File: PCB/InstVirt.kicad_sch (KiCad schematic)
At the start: 45 parts, among them J1 Conn_01x20_Pin, J2 Conn_01x20_Pin, J3 Conn_01x08_Socket, J4 Conn_01x08_Socket, Q1 BC548, Q2 BC548, Q3 BC548, Q4 BC548, Q5 BC548, Q6 BC548, Q7 BC548, Q8 BC548, U1 4051

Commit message: Actualizo circuito PCB
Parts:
- removed Q1, Q2, Q3, Q5, Q6, Q7, Q8: BC548, Package_TO_SOT_THT:TO-92_Inline, symbol Transistor_BJT:BC548
- removed R25, R33, R34, R40, R44: R, symbol Device:R
- removed R26, R35, R37, R41, R46: 10KΩ, symbol Device:R
- added R19, R20, R23: R10KΩ, symbol Device:R
- added U2: ULN2003, symbol Transistor_Array:ULN2003
- R17, R21: value R -> R10KΩ
- R18, R22: value 10KΩ -> R10KΩ
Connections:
- net GND: now also U2.8 (GND)
- net SD1: now also R17.1, U2.16 (O1); no longer R18.1
- net SD2: now also R21.1, U2.15 (O2)
- net SD3: now also R23.1, U2.14 (O3); no longer Q4.1 (C), R30.1
- net SD4: now also R18.1, U2.13 (O4)
- net SD5: now also R20.1, U2.12 (O5); no longer R22.1
- net SD6: now also R19.1, U2.11 (O6)
- net SD8: now also Q4.1 (C), R30.1
- net VCC: now also R17.2, R21.2, R19.2, R20.2, R23.2
- net 1: now reaches R29.1
- net 1: now also U2.1 (I1), U2.2 (I2), U2.3 (I3), U2.4 (I4), U2.5 (I5), U2.6 (I6), U2.7 (I7)
- new net: R22.1, U2.10 (O7)
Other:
- moved on the sheet: J4, Q4, R29, R30

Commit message: actualizacion pcb2
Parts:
- added J5: Conn_01x08_Socket, symbol Connector:Conn_01x08_Socket
- added R24, R27, R31, R33, R35, R37, R39, R41: 10KΩ, symbol Device:R
- added R25, R26, R28, R32, R34, R36, R38, R40: R, symbol Device:R
- added U10, U3, U4, U5, U6, U7, U8, U9: PC817, Package_DIP:DIP-4_W7.62mm, symbol Isolator:PC817
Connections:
- net GND: now also R24.2, R27.2, R31.2, R33.2, R35.2, R37.2, R39.2, R41.2
- net VCC: now also U1.16 (VDD)
- new net: R40.1, U10.1
- new net: R25.1, U3.1
- new net: R36.1, U8.1
- new net: R34.1, U7.1
- new net: R38.1, U9.1
- new net: R26.1, U4.1
- new net: R28.1, U5.1
- new net: R32.1, U6.1
- new net +3.3V: U10.4, U3.4, U4.4, U5.4, U6.4, U7.4, U8.4, U9.4
- new net E1: J5.8 (Pin_8), R25.2
- new net E2: J5.7 (Pin_7), R26.2
- new net E3: J5.6 (Pin_6), R28.2
- new net E4: J5.5 (Pin_5), R32.2
- new net E5: J5.4 (Pin_4), R34.2
- new net E6: J5.3 (Pin_3), R36.2
- new net E7: J5.2 (Pin_2), R38.2
- new net E8: J5.1 (Pin_1), R40.2
- new net GND2: U10.2, U3.2, U4.2, U5.2, U6.2, U7.2, U8.2, U9.2
- new net ID1: R24.1, U3.3
- new net ID2: R27.1, U4.3
- new net ID3: R31.1, U5.3
- new net ID4: R33.1, U6.3
- new net ID5: R35.1, U7.3
- new net ID6: R37.1, U8.3
- new net ID7: R39.1, U9.3
- new net ID8: R41.1, U10.3
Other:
- note added: "ENTRADA DIGITAL 0-5 v"
- moved on the sheet: J1, J2, J4, Q4, R17, R18, R19, R20, R21, R22, R23, R29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

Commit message: actualizacion pcb3
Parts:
- added J6: Conn_01x04, Connector_PinSocket_2.54mm:PinSocket_1x04_P2.54mm_Vertical, symbol Connector_Generic:Conn_01x04
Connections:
- net A6 is gone; now on net A6ADC1_IN6: J1.10 (Pin_10)
- net B12 is gone; now on net B12EN: J2.1 (Pin_1)
- net MUXA is gone; now on net B15MUXA: U1.11 (A)
- net MUXB is gone; now on net B14MUXB: U1.10 (B)
- net MUXC is gone; now on net B13MUXC: U1.9 (C)
- net E1: no longer R25.2
- net E2: no longer R26.2
- net E3: no longer R28.2
- net E4: no longer R32.2
- net E5: no longer R34.2
- net E6: no longer R36.2
- net E7: no longer R38.2
- net E8: no longer R40.2
- net A6ADC1_IN6: now reaches U1.3 (X)
- net B12EN: now reaches U1.6 (Inh)
- removed net 1: R29.1, U2.1 (I1), U2.2 (I2), U2.3 (I3), U2.4 (I4), U2.5 (I5), U2.6 (I6), U2.7 (I7)
- net A0 renamed A0O3
- net A0O3: now also U2.5 (I5)
- net A1 renamed A1O4
- net A1O4: now also U2.4 (I4)
- net A10 renamed A10RX
- net A10RX: now also J6.2 (Pin_2)
- net A15 renamed A15ID8
- net A15ID8: now also R40.2
- net A2 renamed A2O5
- net A2O5: now also U2.3 (I3)
- net A3 renamed A3O6
- net A3O6: now also U2.2 (I2)
- net A4 renamed A4O7
- net A4O7: now also U2.1 (I1)
- net A5 renamed A5O8
- net A5O8: now also R29.1
- net A7 renamed A7OPWM1
- net A8 renamed A8RS_MODE
- net A9 renamed A9TX
- net A9TX: now also J6.3 (Pin_3)
- net B0 renamed B0OPWM2
- net B13 renamed B13MUXC
- net B14 renamed B14MUXB
- net B15 renamed B15MUXA
- net B3 renamed B3ID7
- net B4 renamed B4ID6
- net B4ID6: now also R36.2
- net B5 renamed B5ID5
- net B5ID5: now also R34.2
- net B6 renamed B6ID4
- net B6ID4: now also R32.2
- net B7 renamed B7ID3
- net B7ID3: now also R28.2
- net B8 renamed B8ID2
- net B9 renamed B9ID1
- net B9ID1: now also R25.2
- net C13: no longer names the net of J1.19 (Pin_19)
- net C14 renamed C14O1
- net C14O1: now also U2.7 (I7)
- net C15 renamed C15O2
- net C15O2: now also U2.6 (I6)
- new net B9ID2: R26.2
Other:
- moved on the sheet: Q4, R29, R30

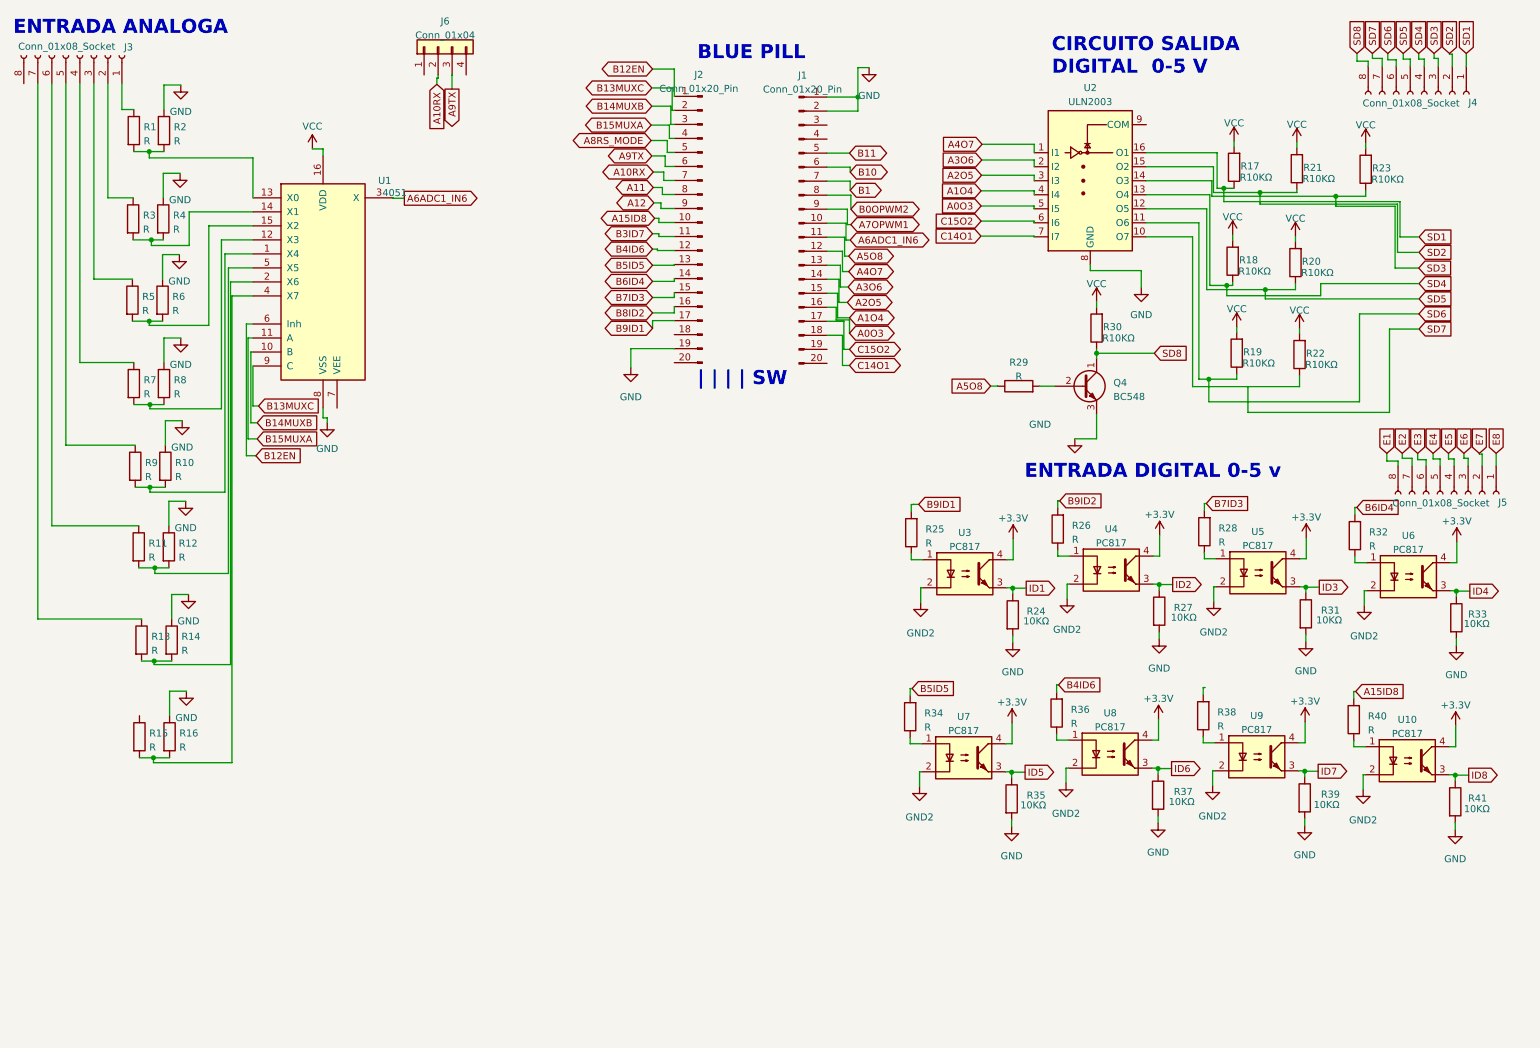
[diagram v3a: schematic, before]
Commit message: Solo faltan entradas analóogicas
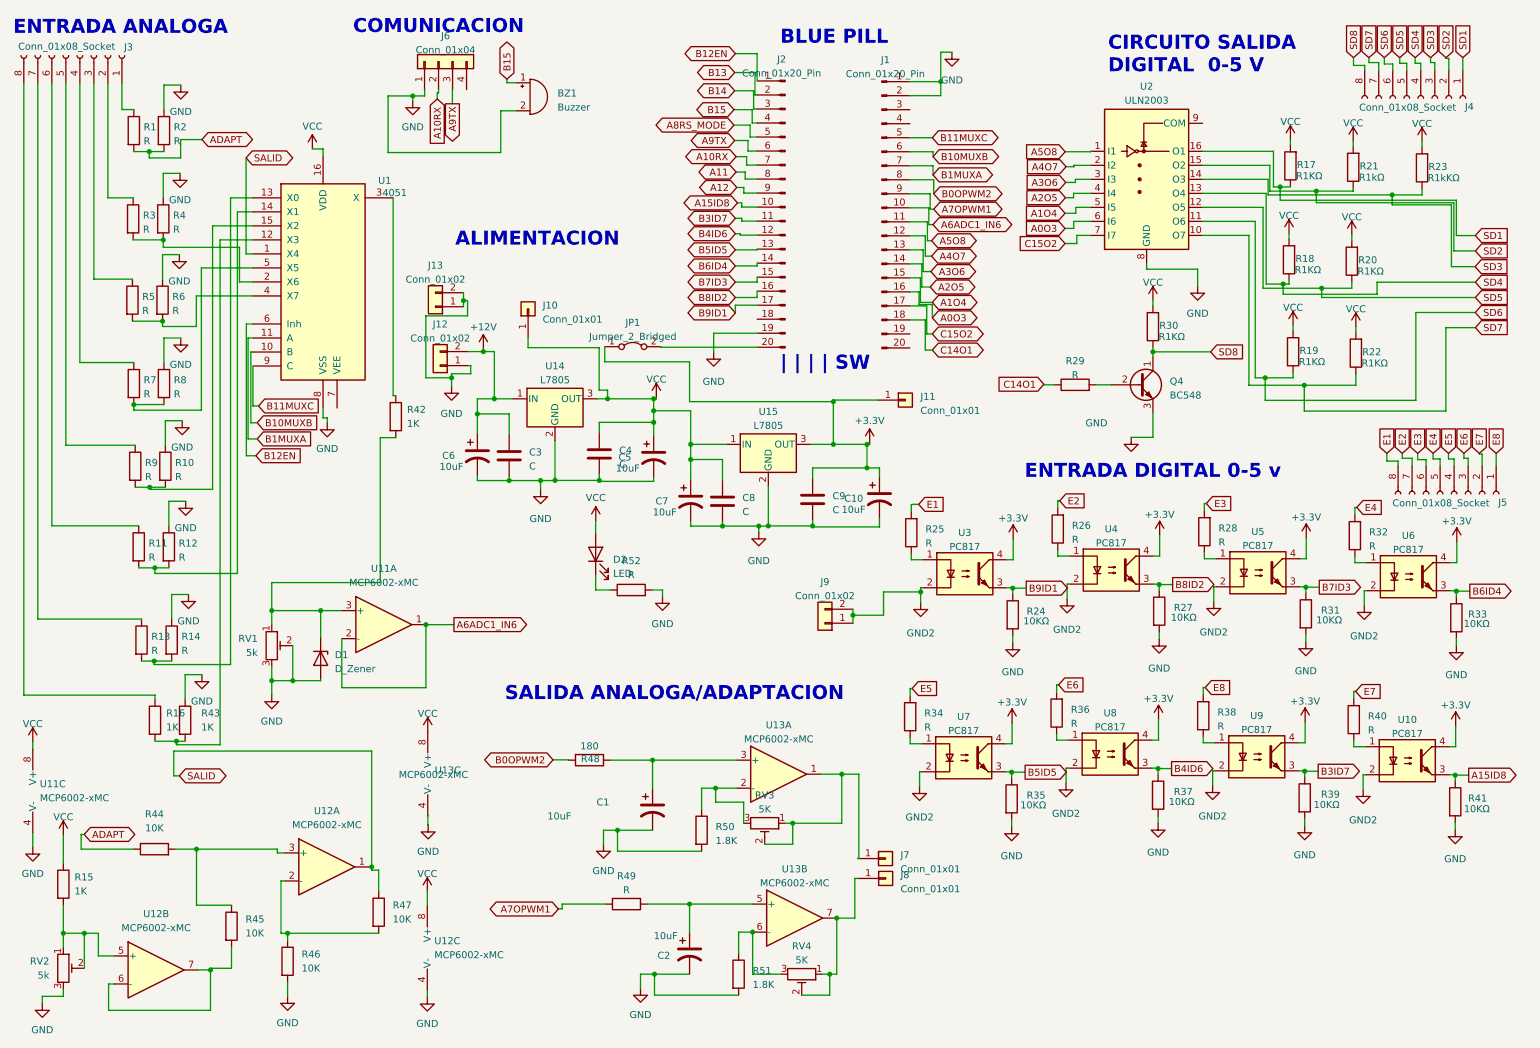
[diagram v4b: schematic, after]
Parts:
- added BZ1: Buzzer, Buzzer_Beeper:MagneticBuzzer_ProSignal_ABI-010-RC, symbol Device:Buzzer
- added C1, C10, C2, C5, C6, C7: 10uF, Capacitor_THT:CP_Radial_D5.0mm_P2.50mm, symbol Device:C_Polarized_US
- added C3, C4, C8, C9: C, Capacitor_THT:C_Disc_D5.0mm_W2.5mm_P5.00mm, symbol Device:C
- added D1: D_Zener, Diode_THT:D_DO-34_SOD68_P10.16mm_Horizontal, symbol Device:D_Zener
- added D2: LED, LED_THT:LED_D5.0mm, symbol Device:LED
- added J10, J11, J7, J8: Conn_01x01, Connector_PinSocket_2.54mm:PinSocket_1x01_P2.54mm_Vertical, symbol Connector_Generic:Conn_01x01
- added J12, J13: Conn_01x02, TerminalBlock_Phoenix:TerminalBlock_Phoenix_MKDS-1,5-2_1x02_P5.00mm_Horizontal, symbol Connector_Generic:Conn_01x02
- added J9: Conn_01x02, Connector_PinSocket_2.54mm:PinSocket_1x02_P2.54mm_Vertical, symbol Connector_Generic:Conn_01x02
- added JP1: Jumper_2_Bridged, Connector_PinSocket_2.54mm:PinSocket_1x02_P2.54mm_Vertical, symbol Jumper:Jumper_2_Bridged
- added R42: 1K, Resistor_SMD:R_1206_3216Metric, symbol Device:R
- added R43: 1K, Resistor_THT:R_Axial_DIN0207_L6.3mm_D2.5mm_P10.16mm_Horizontal, symbol Device:R
- added R44, R45, R46, R47: 10K, Resistor_SMD:R_1206_3216Metric, symbol Device:R
- added R48: 180, Resistor_SMD:R_1206_3216Metric, symbol Device:R
- added R49: R, Resistor_SMD:R_1206_3216Metric, symbol Device:R
- added R50, R51: 1.8K, Resistor_THT:R_Axial_DIN0207_L6.3mm_D2.5mm_P10.16mm_Horizontal, symbol Device:R
- added R52: R, Resistor_THT:R_Axial_DIN0207_L6.3mm_D2.5mm_P10.16mm_Horizontal, symbol Device:R
- added RV1, RV2: 5k, Potentiometer_THT:Potentiometer_Bourns_3296W_Vertical, symbol Device:R_Potentiometer_Trim
- added RV3, RV4: 5K, Potentiometer_THT:Potentiometer_Bourns_3296W_Vertical, symbol Device:R_Potentiometer_Trim
- added U11, U12, U13: MCP6002-xMC, Package_DIP:DIP-8_W7.62mm_LongPads, symbol Amplifier_Operational:MCP6002-xMC
- added U14, U15: L7805, Package_TO_SOT_THT:TO-220-3_Vertical, symbol Regulator_Linear:L7805
- J3, J5: footprint (none) -> Connector_PinHeader_2.54mm:PinHeader_1x08_P2.54mm_Vertical
- J4: footprint (none) -> Connector_PinSocket_2.54mm:PinSocket_1x08_P2.54mm_Vertical
- R1, R11, R13, R24, R27, R3, R31, R33, R35, R37, R39, R41, R5, R7, R9: footprint (none) -> Resistor_SMD:R_1206_3216Metric
- R10, R12, R14, R2, R25, R26, R28, R29, R32, R34, R36, R38, R4, R40, R6, R8: footprint (none) -> Resistor_THT:R_Axial_DIN0207_L6.3mm_D2.5mm_P10.16mm_Horizontal
- R15, R16: value R -> 1K; footprint (none) -> Resistor_SMD:R_1206_3216Metric
- R17, R18, R19, R20, R22, R30: value R10KΩ -> R1KΩ; footprint (none) -> Resistor_SMD:R_1206_3216Metric
- R21: value R10KΩ -> R1kΩ; footprint (none) -> Resistor_SMD:R_1206_3216Metric
- R23: value R10KΩ -> R1kKΩ; footprint (none) -> Resistor_SMD:R_1206_3216Metric
- U1: footprint (none) -> Package_DIP:DIP-16_W7.62mm_LongPads
- U2: footprint (none) -> Package_SO:SOP-16_4.4x10.4mm_P1.27mm
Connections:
- net B9ID2 is gone; now on net E2: R26.2
- net ID1 is gone; now on net B9ID1: R24.1, U3.3
- net ID2 is gone; now on net B8ID2: R27.1, U4.3
- net ID3 is gone; now on net B7ID3: R31.1, U5.3
- net ID4 is gone; now on net B6ID4: R33.1, U6.3
- net ID5 is gone; now on net B5ID5: R35.1, U7.3
- net ID6 is gone; now on net B4ID6: R37.1, U8.3
- net ID7 is gone; now on net B3ID7: R39.1, U9.3
- net ID8 is gone; now on net A15ID8: R41.1, U10.3
- net +3.3V: now also C10.1, C9.1, J11.1 (Pin_1), JP1.1 (A), U15.3 (OUT)
- net A0O3: now also U2.6 (I6); no longer U2.5 (I5)
- net A15ID8: no longer R40.2
- net A1O4: now also U2.5 (I5); no longer U2.4 (I4)
- net A2O5: now also U2.4 (I4); no longer U2.3 (I3)
- net A3O6: now also U2.3 (I3); no longer U2.2 (I2)
- net A4O7: now also U2.2 (I2); no longer U2.1 (I1)
- net A5O8: now also U2.1 (I1); no longer R29.1
- net A6ADC1_IN6: now also U11.1, U11.2 (-); no longer U1.3 (X)
- net A7OPWM1: now also R49.2
- net B0OPWM2: now also R48.2
- net B4ID6: no longer R36.2
- net B5ID5: no longer R34.2
- net B6ID4: no longer R32.2
- net B7ID3: no longer R28.2
- net B9ID1: no longer R25.2
- net C14O1: now also R29.1; no longer U2.7 (I7)
- net C15O2: now also U2.7 (I7); no longer U2.6 (I6)
- net E1: now also R25.2
- net E3: now also R28.2
- net E4: now also R32.2
- net E5: now also R34.2
- net E6: now also R36.2
- net E7: now also R40.2
- net E8: now also R38.2
- net GND: now also J6.1 (Pin_1), BZ1.2 (+), C1.2, C10.2, C2.2, C3.2, C4.2, C5.2, C6.2, C7.2, C8.2, C9.2, D1.2 (A), J12.1 (Pin_1), J13.1 (Pin_1), J13.2 (Pin_2), R43.1, R46.2, R50.2, R51.2, R52.2, RV1.2, RV1.3, RV2.3, U11.4 (V-), U11.9 (V-), U12.4 (V-), U12.9 (V-), U13.4 (V-), U13.9 (V-), U14.2 (GND), U15.2 (GND); no longer R16.1
- net GND2: now also J9.1 (Pin_1), J9.2 (Pin_2)
- net SD7: now also R22.1, U2.10 (O7)
- net VCC: now also R15.1, C4.1, C5.1, C7.1, C8.1, D2.2 (A), J10.1 (Pin_1), U11.8 (V+), U12.8 (V+), U13.8 (V+), U14.3 (OUT), U15.1 (IN)
- net at R3.2, R4.2: now also U1.2 (X6); no longer U1.14 (X1)
- net at R10.2, R9.2: now also U1.15 (X2); no longer U1.1 (X4)
- net at R7.2, R8.2: now also U1.5 (X5); no longer U1.12 (X3)
- net at R5.2, R6.2: now also U1.4 (X7); no longer U1.15 (X2)
- net at J3.8 (Pin_8): now also R16.1
- net at R11.2, R12.2: now also U1.14 (X1); no longer U1.5 (X5)
- net at J2.20 (Pin_20): now also JP1.2 (B)
- net at R13.2, R14.2: now also U1.13 (X0); no longer U1.2 (X6)
- net ADAPT: now reaches R1.2, R2.2
- net ADAPT: now also R44.1; no longer U1.13 (X0)
- net B1 renamed B1MUXA
- net B1MUXA: now also U1.11 (A)
- net B10 renamed B10MUXB
- net B10MUXB: now also U1.10 (B)
- net B11 renamed B11MUXC
- net B11MUXC: now also U1.9 (C)
- net B13MUXC renamed B13 
- net B13 : no longer U1.9 (C)
- net B14MUXB renamed B14 
- net B14 : no longer U1.10 (B)
- net B15MUXA renamed B15 
- net B15 : now also BZ1.1 (-); no longer U1.11 (A)
- new net: R44.2, R45.1, U12.3 (+)
- new net: R45.2, U12.6 (-), U12.7
- new net: R15.2, RV2.1, RV2.2, U12.5 (+)
- new net: J7.1 (Pin_1), RV3.1, RV3.2, U13.1
- new net: R50.1, RV3.3, U13.2 (-)
- new net: C1.1, R48.1, U13.3 (+)
- new net: R46.1, R47.2, U12.2 (-)
- new net: J8.1 (Pin_1), RV4.1, RV4.2, U13.7
- new net: R51.1, RV4.3, U13.6 (-)
- new net: D2.1 (K), R52.1
- new net: R16.2, R43.2, U1.12 (X3)
- new net: C2.1, R49.1, U13.5 (+)
- new net: D1.1 (K), R42.2, RV1.1, U11.3 (+)
- new net: R42.1, U1.3 (X)
- new net +12V: C3.1, C6.1, J12.2 (Pin_2), U14.1 (IN)
- new net SALID: R47.1, U1.1 (X4), U12.1
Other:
- note added: "ALIMENTACION"
- note added: "COMUNICACION"
- note added: "SALIDA ANALOGA/ADAPTACION"
- moved on the sheet: J1, J2, J4, J6, Q4, R17, R18, R19, R20, R21, R22, R23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
